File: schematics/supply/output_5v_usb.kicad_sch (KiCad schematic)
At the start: 80 parts, among them J2 USB_A, Q3 40N06, U10 LM158DR, U11 IP2163, U12 LM158DR, U13 TL432DBZ, U14 LM158DR, U15 LDL1117S33R, U2 EL817, U24 LM1085-3.3, U6 INA3221, U8 MC34063AD, U9 IRS2153S

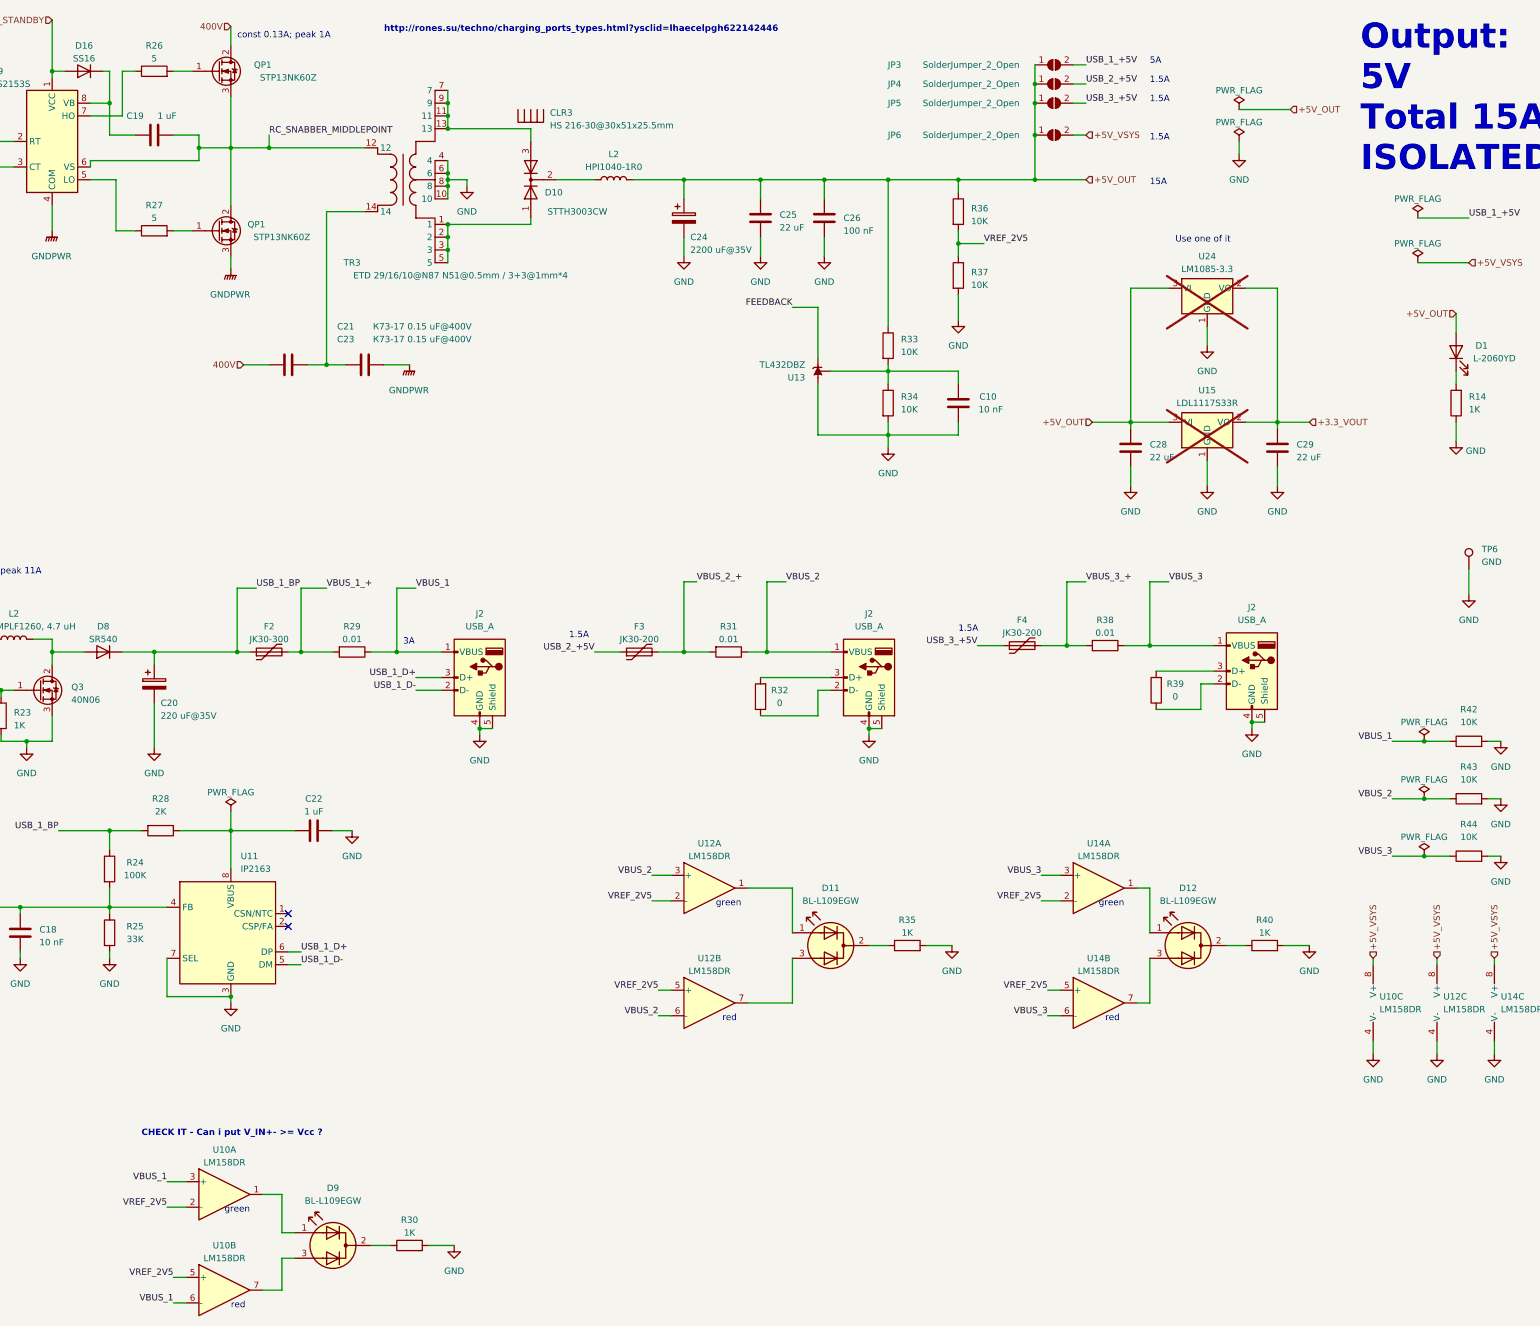
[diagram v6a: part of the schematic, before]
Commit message: Added over-voltage protection to 5V line
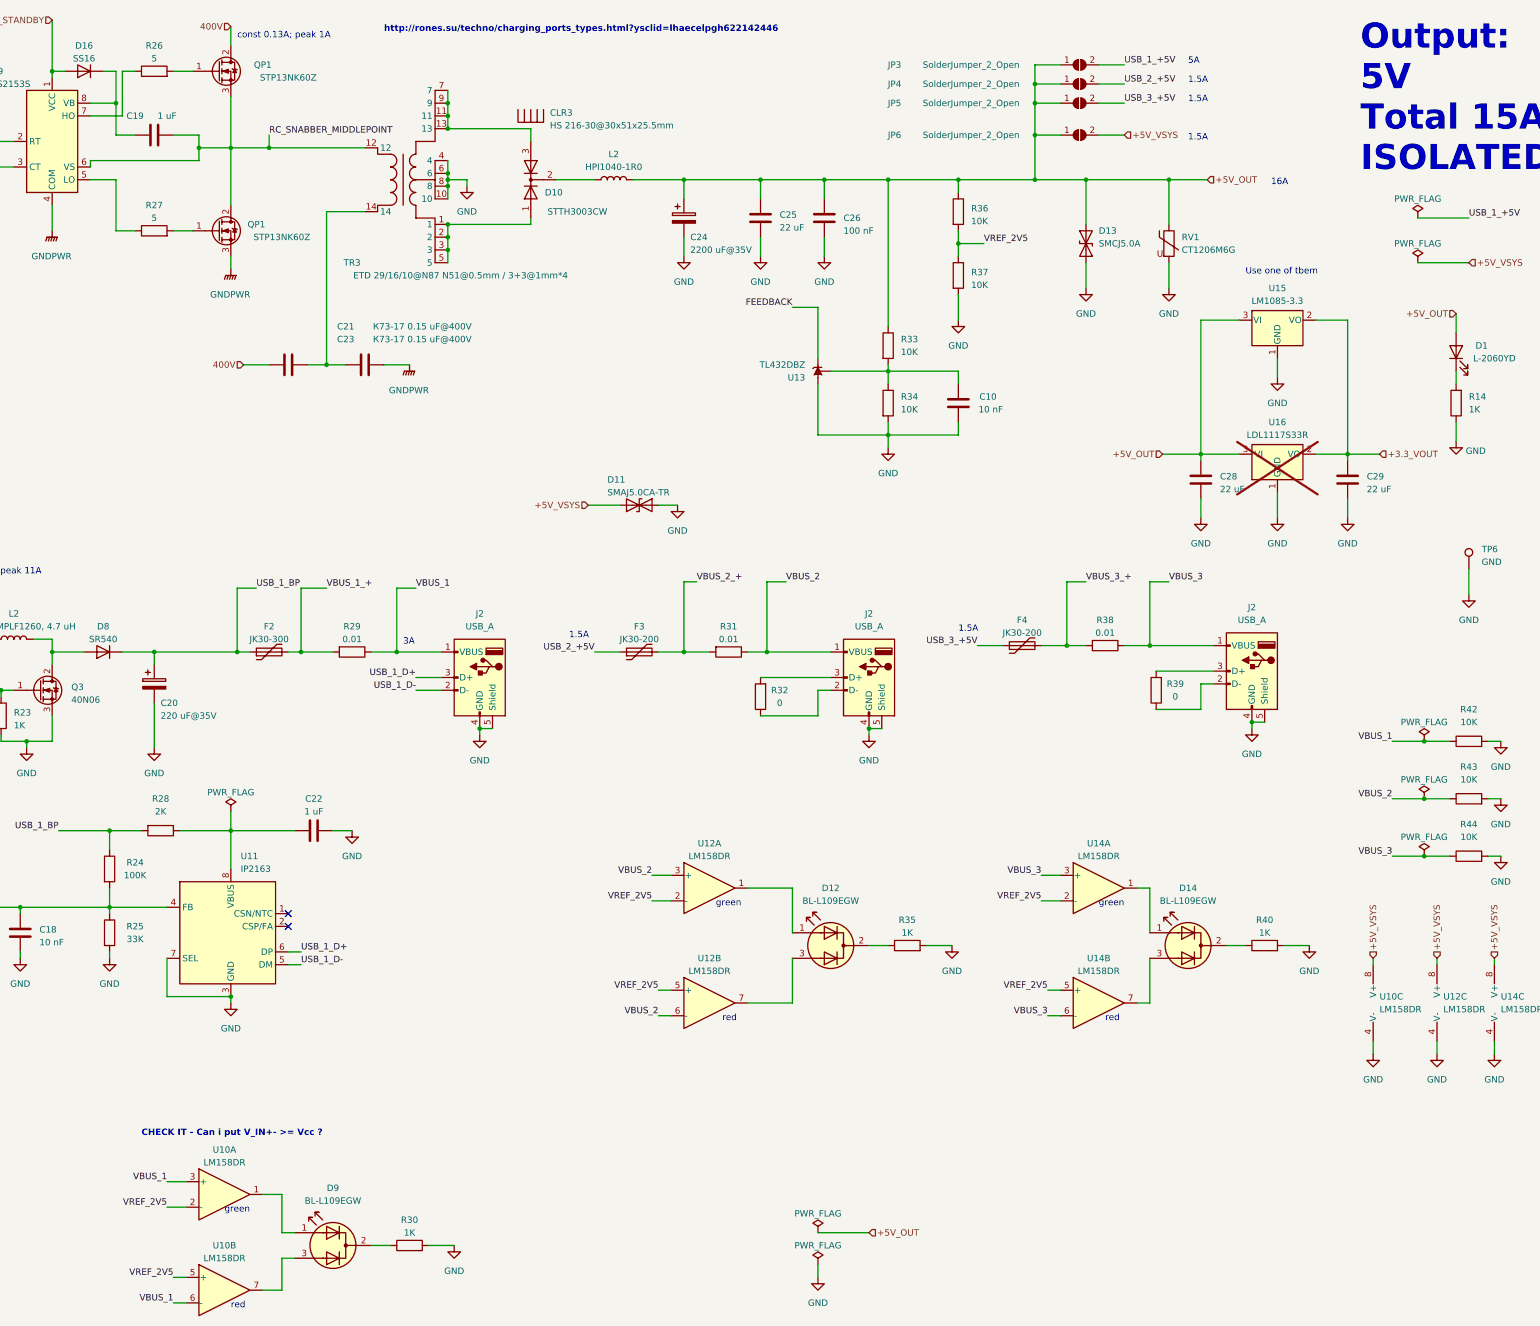
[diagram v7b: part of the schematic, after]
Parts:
- added D11: SMAJ5.0CA-TR, Diode_SMD:D_SMA, symbol Diode:ESD9B3.3ST5G
- added D13: SMCJ5.0A, Diode_SMD:D_SMC, symbol Diode:ESD9B3.3ST5G
- added RV1: CT1206M6G, Resistor_SMD:R_1206_3216Metric, symbol Device:Varistor
- U15: renamed from U24; now fitted; now in the parts list
- renumbered D11 to D12, D12 to D14, U15 to U16
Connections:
- net +5V_OUT: now also D13.2 (A2), RV1.1
- net +5V_VSYS: now also D11.2 (A2)
- net GND: now also D11.1 (A1), D13.1 (A1), RV1.2
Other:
- note added: "16A"
- note added: "Use one of tbem"
- note removed: "15A"
- note removed: "Use one of it"
- moved on the sheet: C28, C29, JP3, JP4, JP5, JP6, U16

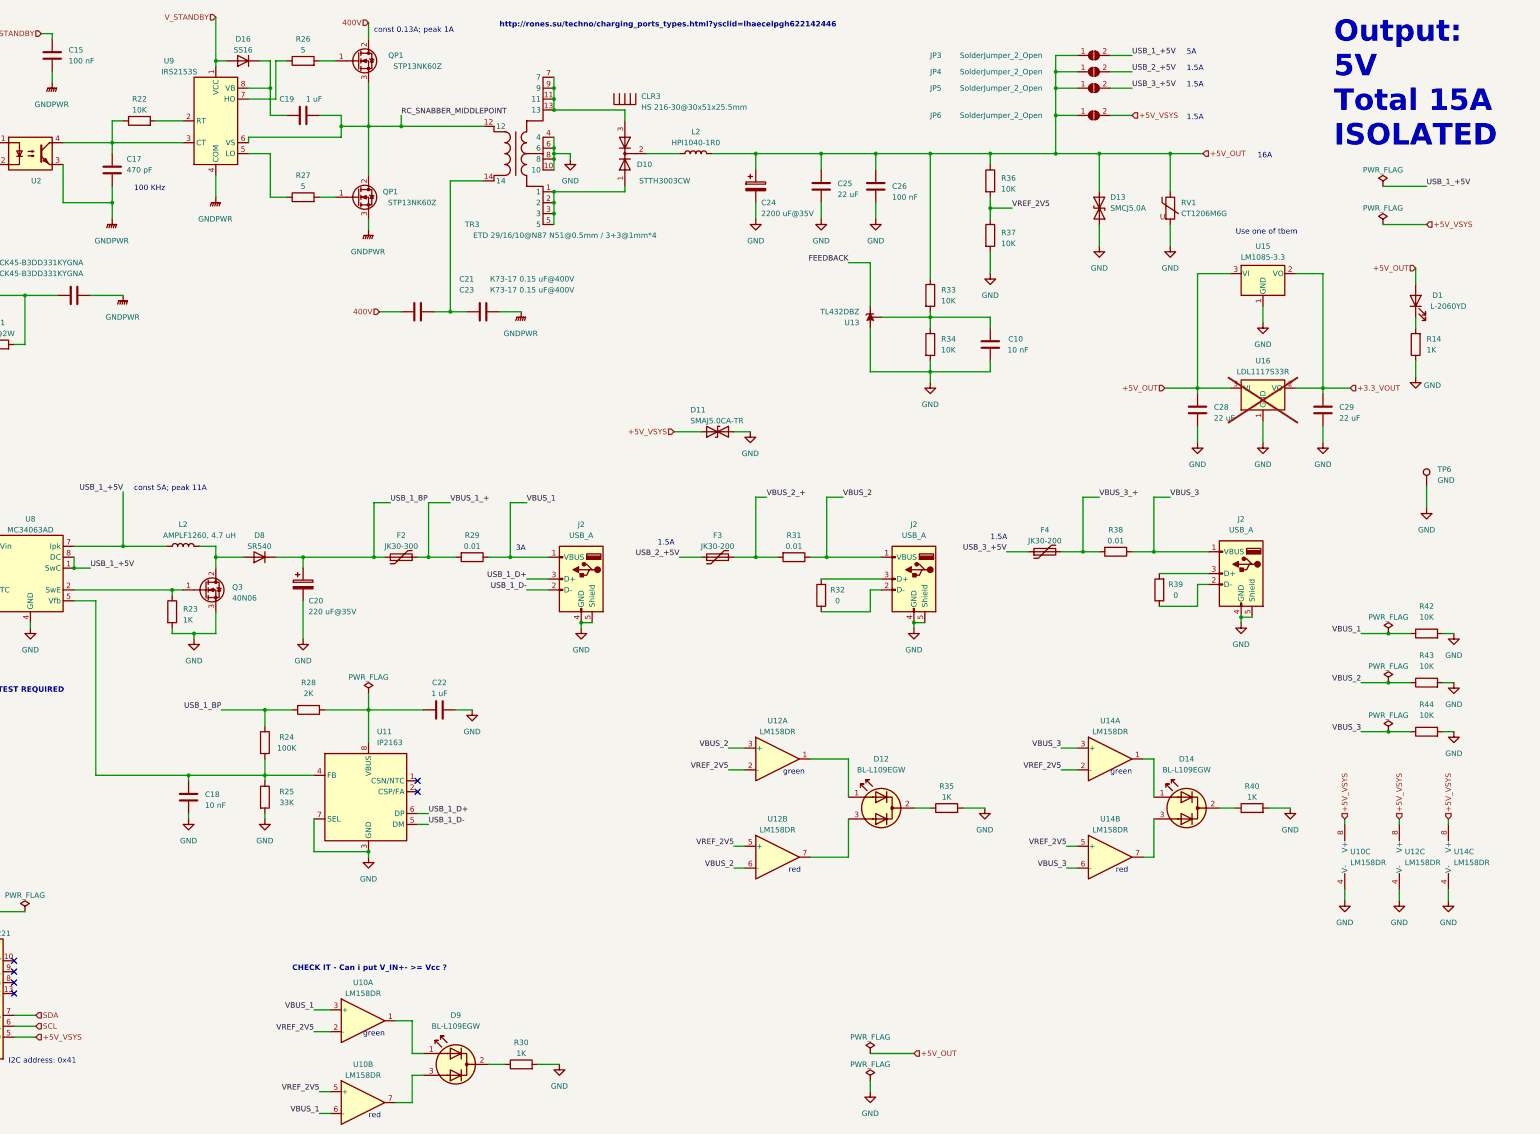
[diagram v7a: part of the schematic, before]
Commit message: Fixed problem with 20V on one leg of comparator
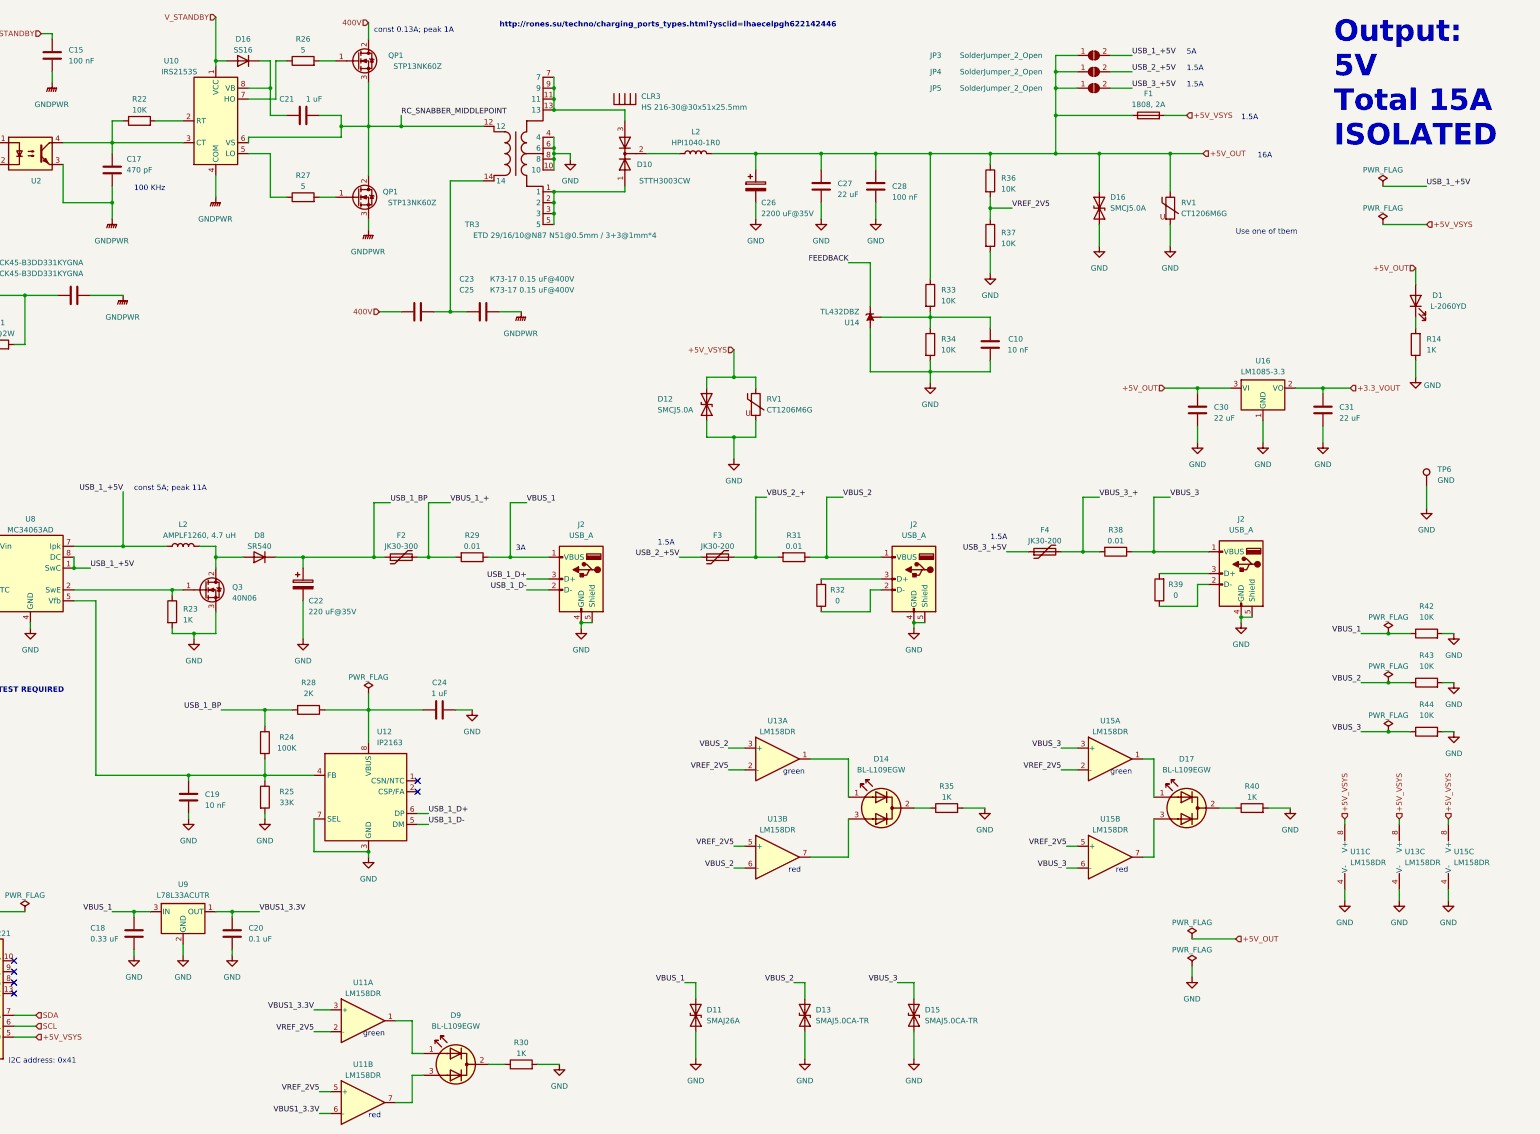
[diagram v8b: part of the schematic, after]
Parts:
- removed JP6: SolderJumper_2_Open, Jumper:SolderJumper-2_P1.3mm_Open_TrianglePad1.0x1.5mm, symbol Jumper:SolderJumper_2_Open
- removed U16: LDL1117S33R, Package_TO_SOT_SMD:SOT-223-3_TabPin2, symbol Regulator_Linear:AMS1117-3.3
- added C18: 0.33 uF, Capacitor_SMD:C_0603_1608Metric, symbol Device:C
- added C20: 0.1 uF, Capacitor_SMD:C_0603_1608Metric, symbol Device:C
- added D12: SMCJ5.0A, Diode_SMD:D_SMC, symbol Diode:ESD9B3.3ST5G
- added D13, D15: SMAJ5.0CA-TR, Diode_SMD:D_SMA, symbol Diode:ESD9B3.3ST5G
- added F1: 1808, 2A, Library:FuseHolder1808, symbol Device:Fuse
- added RV1: CT1206M6G, Resistor_SMD:R_1206_3216Metric, symbol Device:Varistor
- added U9: L78L33ACUTR, Package_TO_SOT_SMD:SOT-89-3, symbol Regulator_Linear:L78L33_SOT89
- D11: value SMAJ5.0CA-TR -> SMAJ26A
- renumbered C18 to C19, C19 to C21, C20 to C22, C21 to C23, C22 to C24, C23 to C25, C24 to C26, C25 to C27, C26 to C28, C28 to C30, C29 to C31, D12 to D14, D13 to D16, D14 to D17, U9 to U10, U10 to U11, U11 to U12, U12 to U13, U13 to U14, U14 to U15, U15 to U16
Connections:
- net +5V_OUT: now also F1.1
- net +5V_VSYS: now also D12.2 (A2), F1.2, RV1.1; no longer D11.2 (A2)
- net GND: now also C18.1, C20.1, D12.1 (A1), D13.1 (A1), D15.1 (A1), RV1.2, U9.2 (GND)
- net VBUS_1: now also D11.2 (A2), C18.2, U9.3 (IN); no longer U11.3 (+), U11.6 (-)
- net VBUS_2: now also D13.2 (A2)
- net VBUS_3: now also D15.2 (A2)
- new net VBUS1_3.3V: C20.2, U11.3 (+), U11.6 (-), U9.1 (OUT)
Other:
- note removed: "CHECK IT - Can i put V_IN+- >= Vcc ?"
- moved on the sheet: U16
